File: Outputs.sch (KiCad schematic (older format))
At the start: 21 parts

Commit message: Agrego v1.0 de SmartSaffron
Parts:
- removed C?: C, symbol Device:C
- removed Q?: Mac97a8, symbol 00_lib_sch:Triac_Thyristor_Mac97a8
- removed Q?: Q_NMOS_DGS, symbol Device:Q_NMOS_DGS
- removed R?: 470, symbol Device:R
- removed R? (x2): 1k, symbol Device:R
- removed R?: R, symbol Device:R
- removed U?: MOC3043, symbol 00_lib_sch:MOC3041M
- added C401, C402, C403, C404, C407, C408, C409, C410: 100n, 00_lib_fp:C_0805_2012Metric_Pad1.18x1.45mm_HandSolder, symbol 00_lib_sch:C
- added Q401, Q402, Q405, Q406, Q409, Q410, Q413, Q414: bss138, 00_lib_fp:SOT-23, symbol 00_lib_sch:Q_NMOS_DGS
- added Q403, Q404, Q407, Q408, Q411, Q412, Q415, Q416: mac97a8, 00_lib_fp:TO-92_Inline, symbol 00_lib_sch:Mac97a8
- added R401, R402, R405, R407, R417, R418, R421, R423, R425, R426, R429, R431, R433, R434, R437, R439: 1k, 00_lib_fp:R_0805_2012Metric_Pad1.20x1.40mm_HandSolder, symbol 00_lib_sch:R
- added R403, R404, R406, R408, R419, R420, R422, R424, R427, R428, R430, R432, R435, R436, R438, R440: 470, 00_lib_fp:R_0805_2012Metric_Pad1.20x1.40mm_HandSolder, symbol 00_lib_sch:R
- added U401, U402, U404, U405, U406, U407, U408, U409: MOC3043, 00_lib_fp:DIP-6_W7.62mm_LongPads, symbol 00_lib_sch:MOC3043
- C405: renamed from C?; footprint (none) -> 00_lib_fp:C_0805_2012Metric_Pad1.18x1.45mm_HandSolder; symbol Device:CP1 -> 00_lib_sch:CP1
- C406: renamed from C?; footprint (none) -> 00_lib_fp:C_0805_2012Metric_Pad1.18x1.45mm_HandSolder; symbol Device:C -> 00_lib_sch:C
- J401: renamed from J?; value Screw_Terminal_01x08 -> OUTPUT_SW; footprint (none) -> 00_lib_fp:TerminalBlock_Phoenix_MKDS-1,5-8-5.08_1x08_P5.08mm_Horizontal; symbol Connector:Screw_Terminal_01x08 -> 00_lib_sch:Screw_Terminal_01x08
- J402: renamed from J?; value Screw_Terminal_01x02 -> COMMON; footprint (none) -> 00_lib_fp:TerminalBlock_Phoenix_MKDS-1,5-2-5.08_1x02_P5.08mm_Horizontal; symbol Connector:Screw_Terminal_01x02 -> 00_lib_sch:Screw_Terminal_01x02
- R409, R410, R411, R412, R413, R414, R415, R416: renamed from R?; footprint (none) -> 00_lib_fp:R_0805_2012Metric_Pad1.20x1.40mm_HandSolder; symbol Device:R -> 00_lib_sch:R
- U403: renamed from U?; symbol 00_lib_sch:Interface_Expansion_PCF8574 -> 00_lib_sch:PCF8574
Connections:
- net labels added: 24VAC, AGND, OUT_1, OUT_2, OUT_3, OUT_4, OUT_5, OUT_6, OUT_7, OUT_8, SCA, SCL, [24VAC_outputs], [AGND_outputs]
- net labels removed: [24VAC_in], [AGND]
- wire segments 63 -> 229
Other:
- note added: "OUTPUTS"
- note removed: "Si 24VAC es FASE y Si llamamos \nAGND = NEUTRO entonces está bien"
- moved on the sheet: C405

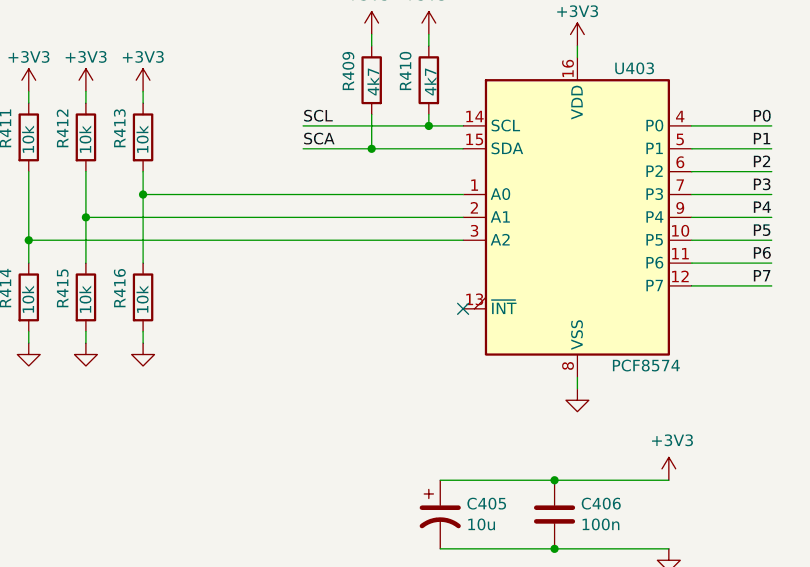
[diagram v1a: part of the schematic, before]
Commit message: Fixes PCB, reset esp32
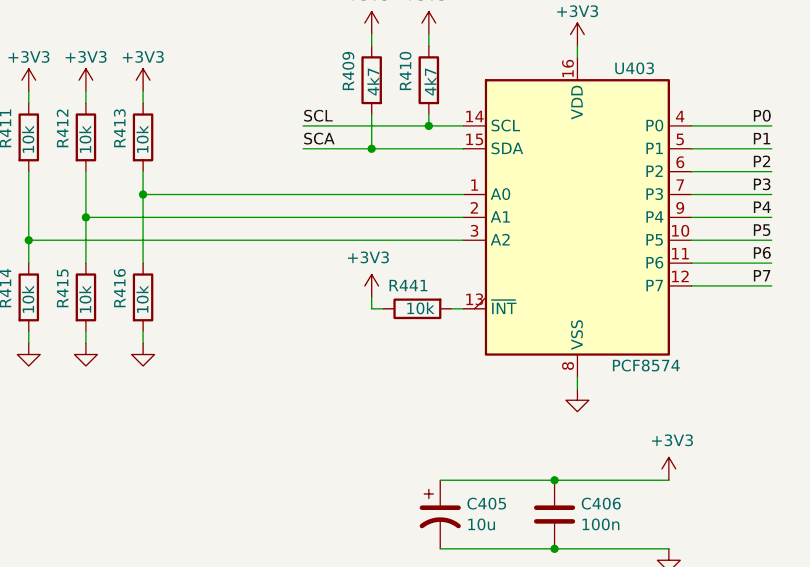
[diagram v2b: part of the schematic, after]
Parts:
- added R441: 10k, 00_lib_fp:R_0805_2012Metric_Pad1.20x1.40mm_HandSolder, symbol 00_lib_sch:R
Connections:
- net +3V3: now also R441.1
- net at U403.13 (~INT~): now also R441.2
- no-connect marks 1 -> 0
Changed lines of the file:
@@
 Wire Wire Line
 	6500 3900 6850 3900
-NoConn ~ 5500 4000
 $Comp
 L 00_lib_sch:Screw_Terminal_01x02 J402
@@
 Text Label 6850 3600 2    50   ~ 0
 P4
+$Comp
+L 00_lib_sch:R R?
+U 1 1 61686280
+P 5300 4000
+AR Path="/61438B2D/61686280" Ref="R?"  Part="1"
+AR Path="/61434A7C/61686280" Ref="R441"  Part="1"
+F 0 "R441" V 5200 3950 50  0000 L CNN
+F 1 "10k" V 5300 3925 50  0000 L CNN
+F 2 "00_lib_fp:R_0805_2012Metric_Pad1.20x1.40mm_HandSolder" V 5230 4000 50  0001 C CNN
+F 3 "~" H 5300 4000 50  0001 C CNN
+	1    5300 4000
+	0    -1   1    0
+$EndComp
+Wire Wire Line
+	5500 4000 5450 4000
+$Comp
+L 00_lib_sch:+3.3V #PWR?
+U 1 1 61695849
+P 5100 3950
+AR Path="/61438B2D/61695849" Ref="#PWR?"  Part="1"
+AR Path="/61434A7C/61695849" Ref="#PWR0247"  Part="1"
+F 0 "#PWR0247" H 5100 3800 50  0001 C CNN
+F 1 "+3V3" H 5115 4123 50  0000 C CNN
+F 2 "" H 5100 3950 50  0001 C CNN
+F 3 "" H 5100 3950 50  0001 C CNN
+	1    5100 3950
+	-1   0    0    -1
+$EndComp
+Wire Wire Line
+	5150 4000 5100 4000
+Wire Wire Line
+	5100 4000 5100 3950
 $EndSCHEMATC
